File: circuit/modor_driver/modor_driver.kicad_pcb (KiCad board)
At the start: 2 copper layers, 50 x 50 mm, 26 parts, among them J1 ZH, J2 ZH, J3 pogo pin, J4 PH, J5 XH, J6 PA, J7 XT_pad, J8 XT_pad, SW1 SW_Push, U2 STM32C011F4Px

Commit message: レイアウト
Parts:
- added D3: LED_Small, LED_SMD:LED_0603_1608Metric_Pad1.05x0.95mm_HandSolder, F.Cu at (141.5, 61.0)
- added R3: 10k, Resistor_SMD:R_0603_1608Metric_Pad0.98x0.95mm_HandSolder, F.Cu at (141.5, 64.0)
- R2: moved to F.Cu
- moved C6 49.7 mm to (138.0, 62.0), turned to 180 degrees
- moved C1 35.8 mm to (123.5, 111.0)
- moved R2 32.9 mm to (130.1, 96.5), turned to 0 degrees
- moved R1 31.6 mm to (127.1, 118.0)
- moved J6 28.0 mm to (140.5, 68.0), turned to 180 degrees
- moved J8 27.1 mm to (131.0, 62.5)
- moved REF** 26.8 mm to (141.0, 56.5)
- moved J7 26.2 mm to (124.5, 62.5)
- moved C2 26.1 mm to (136.8, 119.0)
- moved C3 25.4 mm to (133.0, 111.0)
- moved C5 24.2 mm to (137.1, 96.5)
- moved REF** 22.9 mm to (141.0, 125.5)
- moved D2 22.0 mm to (133.6, 96.5)
- moved C4 21.1 mm to (130.5, 101.5), turned to 90 degrees
- moved D1 19.6 mm to (123.1, 118.0)
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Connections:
- net Net-(J7-Pin_2) renamed +BATT
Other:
- board size 50 x 50 mm -> 22.5 x 74 mm

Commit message: レイアウト変える
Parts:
- moved U1 20.2 mm to (135.8, 100.5), turned to -90 degrees
- moved C2 17.9 mm to (138.5, 101.2), turned to 90 degrees
- moved C4 13.1 mm to (133.7, 114.2), turned to -90 degrees
- moved C1 12.5 mm to (131.7, 101.6)
- moved C3 7.43 mm to (138.5, 106.0), turned to -90 degrees
- moved U2 7.34 mm to (133.7, 106.6), turned to 180 degrees
- moved J7 6.18 mm to (126.0, 68.5), turned to 0 degrees
- moved J8 5.02 mm to (126.0, 62.0), turned to 0 degrees
- moved R1 4.26 mm to (123.1, 119.5)
- moved J6 4.00 mm to (136.5, 68.1), turned to 0 degrees
- moved R3 3.50 mm to (141.5, 60.5), turned to 0 degrees
- moved D3 2.50 mm to (141.5, 63.5), turned to 0 degrees
- moved C6 1.41 mm to (137.0, 63.0), turned to 90 degrees
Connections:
- J1 pad 3: /SPI_MISO -> /SPI_CS
- J1 pad 4: /SPI_MOSI -> /SPI_MISO
- J1 pad 5: /SPI_CS -> /SPI_MOSI
- J2 pad 3: /SPI_MISO -> /SPI_CS
- J2 pad 4: /SPI_MOSI -> /SPI_MISO
- J2 pad 5: /SPI_CS -> /SPI_MOSI
- J3 pad 2: /SWCLK -> /SWDIO
- J3 pad 3: /SWDIO -> /SWCLK
- J4 pad 2: /UART_TX -> /UART_RX
- J4 pad 3: /UART_RX -> /UART_TX
- U2 pad 1: /ENCODER_A -> /ENCODER_B
- U2 pad 14: /ENCODER_B -> /ENCODER_A
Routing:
- net GND: track 0.00 -> 106.9 mm
- net +3V3: track 0.00 -> 37.4 mm
- net /NRST: track 0.00 -> 32.4 mm, vias 0 -> 1
- net +BATT: track 0.00 -> 30.7 mm
- net /SWDIO: track 0.00 -> 28.2 mm
- net /SWCLK: track 0.00 -> 27.9 mm
- net Net-(J6-Pin_1): track 0.00 -> 24.4 mm
- net Net-(J6-Pin_2): track 0.00 -> 21.1 mm
- net Net-(J6-Pin_3): track 0.00 -> 17.0 mm
- net /SPI_SCK: track 0.00 -> 13.2 mm
- net /SPI_MOSI: track 0.00 -> 13.1 mm
- net /ENCODER_A: track 0.00 -> 12.6 mm, vias 0 -> 1
- net /SPI_MISO: track 0.00 -> 10.1 mm
- net /SPI_CS: track 0.00 -> 9.84 mm
- net /UART_TX: track 0.00 -> 9.64 mm, vias 0 -> 1
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
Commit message: いったんやりきった
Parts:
- C1, C2, C3, C5, R1, U1, U2: moved to F.Cu
- moved J4 20.8 mm to (140.7, 115.7), turned to 180 degrees
- moved C5 14.9 mm to (123.1, 101.4), turned to 0 degrees
- moved SW1 14.2 mm to (125.5, 105.0), turned to 180 degrees
- moved D2 10.7 mm to (123.1, 98.4)
- moved C4 9.35 mm to (132.0, 105.0), turned to 0 degrees
- moved J5 8.77 mm to (135.5, 99.3), turned to 180 degrees
- moved C1 8.20 mm to (133.5, 109.6), turned to -90 degrees
- moved R2 7.77 mm to (123.1, 99.9)
- moved J1 7.68 mm to (130.7, 115.3), turned to 180 degrees
- moved U2 5.96 mm to (139.4, 108.3), turned to -90 degrees
- moved J2 5.90 mm to (130.6, 110.7), turned to 180 degrees
- moved U1 5.12 mm to (140.8, 100.9), turned to 180 degrees
- moved C2 3.49 mm to (140.4, 98.3), turned to 0 degrees
- moved C3 2.68 mm to (139.7, 103.6), turned to 180 degrees
- moved R1 2.02 mm to (124.4, 118.0)
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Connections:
- J1 pad 2: /SPI_SCK -> /SPI_CS
- J1 pad 3: /SPI_CS -> /SPI_SCK
- J2 pad 2: /SPI_SCK -> /SPI_CS
- J2 pad 3: /SPI_CS -> /SPI_SCK
- J3 pad 2: /SWDIO -> /NRST
- J3 pad 4: /NRST -> /SWDIO
- J4 pad 2: /UART_RX -> /UART_TX
- J4 pad 3: /UART_TX -> /UART_RX
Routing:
- net GND: track 106.9 -> 191.2 mm, vias 0 -> 63
- net /PWM1: track 0.00 -> 42.7 mm, vias 0 -> 1
- net /PWM2: track 0.00 -> 36.0 mm, vias 0 -> 1
- net /PWM3: track 0.00 -> 33.5 mm, vias 0 -> 1
- net /MOTOR_EN: track 0.00 -> 30.0 mm, vias 0 -> 1
- net /LED: track 0.00 -> 23.8 mm, vias 0 -> 2
- net +3V3: track 37.4 -> 54.5 mm, vias 0 -> 1
- net /ENCODER_A: track 12.6 -> 28.6 mm
- net /SWDIO: track 28.2 -> 12.8 mm, vias 0 -> 1
- net /SPI_MOSI: track 13.1 -> 27.1 mm
- net /SWCLK: track 27.9 -> 16.9 mm, vias 0 -> 1
- net /NRST: track 32.4 -> 43.1 mm, vias 1 -> 2
- net /SPI_MISO: track 10.1 -> 20.3 mm
- net /ENCODER_B: track 8.27 -> 17.0 mm
- net /SPI_CS: track 9.84 -> 15.2 mm
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- added copper zone on B.Cu, net GND
- added copper zone on F.Cu, net GND
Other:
- outline, holes or cut-outs redrawn

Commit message: いったん完成
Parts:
- SW1: value SW_Push -> SW_MEC_5E; footprint Button_Switch_SMD:SW_SPST_SKQG_WithStem -> Button_Switch_SMD:SKRPACE010
- moved SW1 2.56 mm to (127.9, 106.0)
- moved R1 1.90 mm to (126.3, 118.0)
- moved D1 1.31 mm to (122.9, 117.9), turned to 0 degrees
- moved J3 0.30 mm to (128.4, 120.8)
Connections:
- J3 pad 3: /SWCLK -> /SWDIO
- J3 pad 4: /SWDIO -> /SWCLK
- SW1 pad 2: /NRST -> GND
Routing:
- net GND: track 191.2 -> 202.2 mm, vias 63 -> 129
- net /SWCLK: track 16.9 -> 13.4 mm
- net /SWDIO: track 12.8 -> 15.9 mm
- net +3V3: track 54.5 -> 56.8 mm
- net /NRST: track 43.1 -> 41.8 mm
- net /PWM3: track 33.5 -> 34.5 mm

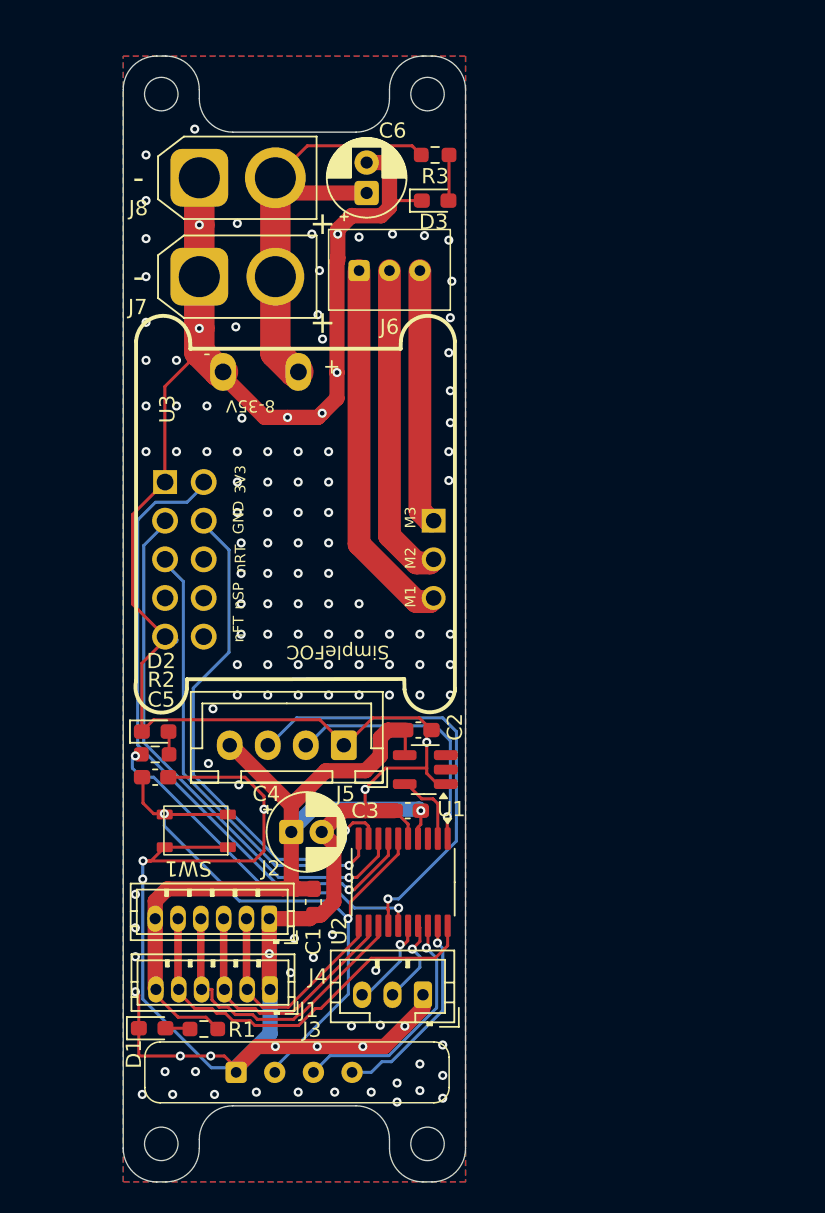
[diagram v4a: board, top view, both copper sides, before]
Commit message: コネクタ変更とsimplefocminiを修正
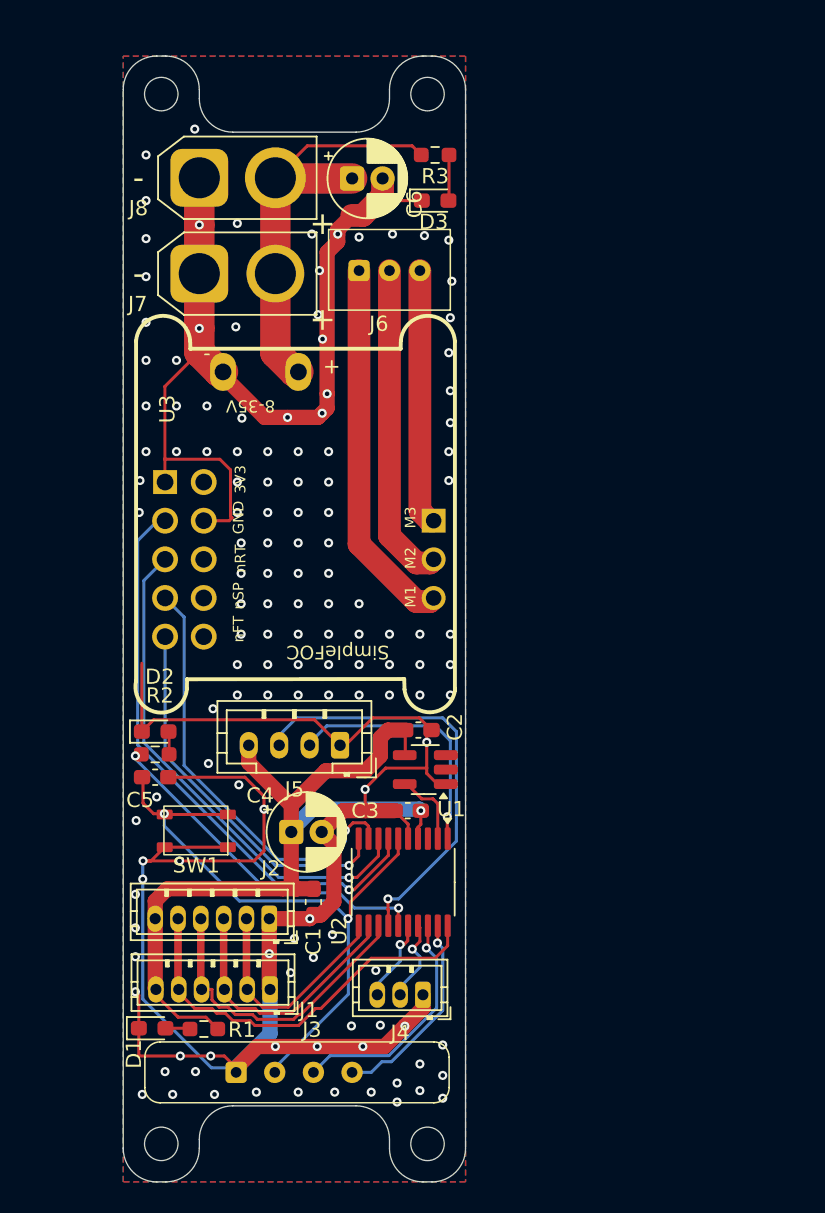
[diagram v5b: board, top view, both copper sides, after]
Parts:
- J4: value PH -> ZH; footprint Connector_JST:JST_PH_B3B-PH-K_1x03_P2.00mm_Vertical -> Connector_JST:JST_ZH_B3B-ZR_1x03_P1.50mm_Vertical
- J5: value XH -> PH; footprint Connector_JST:JST_XH_B4B-XH-A_1x04_P2.50mm_Vertical -> Connector_JST:JST_PH_B4B-PH-K_1x04_P2.00mm_Vertical
- moved C6 1.35 mm to (136.0, 62.0), turned to 0 degrees
- moved J5 0.25 mm to (135.2, 99.3)
- moved J7 0.20 mm to (126.0, 68.3)
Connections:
- U3 pad 2: /PWM1 -> unconnected-(U3-3V3-Pad2)
- U3 pad 3: /PWM2 -> /PWM1
- U3 pad 4: /PWM3 -> GND
- U3 pad 5: /MOTOR_EN -> /PWM2
- U3 pad 7: unconnected-(U3-nSP-Pad7) -> /PWM3
- U3 pad 9: GND -> /MOTOR_EN
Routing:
- net GND: track 202.2 -> 193.8 mm, vias 129 -> 135
- net /PWM3: track 34.5 -> 28.5 mm
- net /MOTOR_EN: track 30.0 -> 25.5 mm
- net /PWM1: track 42.7 -> 38.5 mm
- net /PWM2: track 36.0 -> 33.7 mm
- net /LED: track 23.8 -> 23.2 mm
- net /UART_RX: track 6.11 -> 5.52 mm
- net +3V3: track 56.8 -> 56.2 mm

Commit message: logo追加
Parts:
- added G***: LOGO, Symbol:sh_5mm, B.Cu at (124.4, 120.1)
